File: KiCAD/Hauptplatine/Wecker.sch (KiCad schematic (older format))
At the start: 4 parts

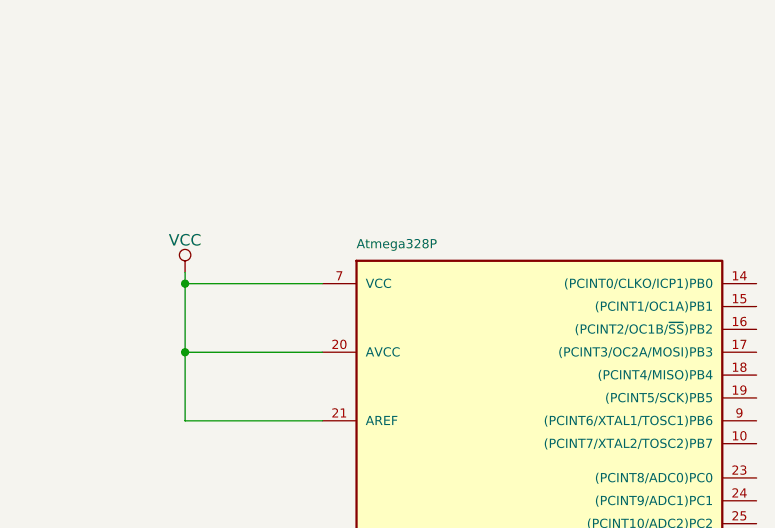
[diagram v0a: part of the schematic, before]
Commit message: Displayplatine Schematic erstellt
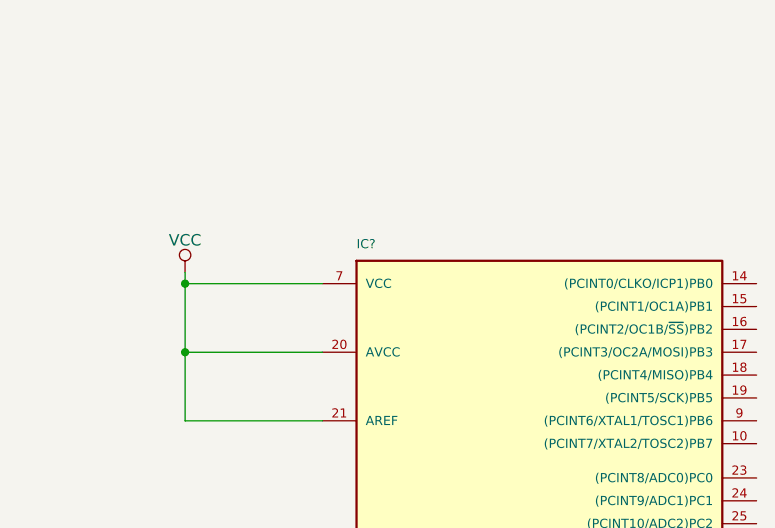
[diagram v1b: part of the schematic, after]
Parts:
- renumbered Atmega328P to IC?
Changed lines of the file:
@@
 $EndDescr
 $Comp
-L ATMEGA328P-P Atmega328P
+L ATMEGA328P-P IC?
 U 1 1 5627CFEE
 P 5750 3150
-F 0 "Atmega328P" H 5000 4400 40  0000 L BNN
+F 0 "IC?" H 5000 4400 40  0000 L BNN
 F 1 "ATMEGA328P-P" H 6150 1750 40  0000 L BNN
 F 2 "DIL28" H 5750 3150 30  0000 C CIN

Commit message: Hauptplatine inkl TDA7266
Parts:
- removed 33µ: C, symbol C
- added C? (x4): 100n, symbol C
- added C?: 33µ, symbol CP
- added P?: CONN_01X02, symbol CONN_01X02
- added P?: CONN_01X05, symbol CONN_01X05
- added P?: CONN_01X08, symbol CONN_01X08
- added R? (x4): R, symbol R
- added U?: TDA7266, TO220-15, symbol TDA7266
- C?: renamed from 47µ; value C -> 0,47µ
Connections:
- net GND: now also C?.1, C?.1, C?.1, C?.1, C?.2, R?.1, R?.1, R?.1, R?.1
- net VCC: now also C?.1, P?.2 (P2)
- net OSC2: now reaches IC?.10 ((PCINT7/XTAL2/TOSC2)PB7)
- net T1.1: now reaches IC?.15 ((PCINT1/OC1A)PB1)
- net T1.1: now also C?.2, P?.1 (P1), R?.2
- net DE-A: now reaches IC?.16 ((PCINT2/OC1B/~SS~)PB2)
- net DE-A: now also C?.2, P?.1 (P1), R?.2
- net DE-B: now reaches IC?.17 ((PCINT3/OC2A/MOSI)PB3)
- net DE-B: now also C?.2, P?.3 (P3), R?.2
- net DE-D: now reaches IC?.18 ((PCINT4/MISO)PB4)
- net DE-D: now also C?.2, P?.4 (P4), R?.2
- net DISP-A0: now reaches IC?.23 ((PCINT8/ADC0)PC0)
- net DISP-A0: now also IC?.26 ((PCINT11/ADC3)PC3), P?.3 (P3)
- net DISP-SCL: now reaches IC?.24 ((PCINT9/ADC1)PC1)
- net DISP-SCL: now also IC?.27 ((PCINT12/SDA/ADC4)PC4), P?.2 (P2)
- net DISP-SI: now reaches IC?.25 ((PCINT10/ADC2)PC2)
- net DISP-SI: now also IC?.28 ((PCINT13/SCL/ADC5)PC5), P?.1 (P1)
- net OSC1: now reaches IC?.9 ((PCINT6/XTAL1/TOSC1)PB6)
- new net DE-C: P?.2 (P2)
- new net DE-E: P?.5 (P5)
- new net DISP-CS1B: P?.5 (P5)
- new net DISP-GND: P?.7 (P7)
- new net DISP-LED: P?.6 (P6)
- new net DISP-RST: P?.4 (P4)
- new net DISP-VCC: P?.8 (P8)

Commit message: Layout Hauptplatine2 v1. Mp3Player-On falsch
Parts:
- removed C?: 100n, symbol C
- removed R?: R, symbol R
- added C10: 470uF, symbol CP
- added C11, C12: 0,22u, symbol C
- added C4: 100n, symbol C
- added C7, C8: 220nF, symbol CP
- added C9: 100nF, symbol C
- added P2: CONN_MP3Player, symbol CONN_01X08
- added P3: LED_Bilder, symbol CONN_01X02
- added P7, P8: CONN_01X02, symbol CONN_01X02
- added P9: CONN_OSC, symbol CONN_01X02
- added R3: R, symbol R
- added R5, R6, R7: 10k, symbol R
- added R8: 220, symbol R
- added U3: LM317T, symbol LM317T
- added U4: CBP, CBP:testneu, symbol CBP
- added U5: CBP, symbol CBP
- IC1: renamed from IC?; footprint DIL28 -> (none)
- P4: renamed from P?; value CONN_01X02 -> CONN_TASTER
- P5: renamed from P?; value CONN_01X05 -> CONN_DREHENCODER
- P6: renamed from P?; value CONN_01X08 -> CONN_DISPLAY
- U2: renamed from U?; footprint TO220-15 -> (none)
- gave numbers to parts that had none: 9
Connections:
- net labels added: Amp-Mute, Amp-Power, LED-Bilder, MP3-L, MP3-R, MP3-T1, MP3-T3, MP3-T4, MP3-T5, MP3_ON1, MP3_ON2, MP3_T1, MP3_T3, MP3_T4, MP3_T5, MP3_VCC, SPK-L+, SPK-L-, SPK-R+, SPK-R-, Transistor-Emitter, Transistorschaltung
- net labels removed: OSC1, OSC2
- wire segments 94 -> 174
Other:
- note added: "Audio-Verstärker"
- note added: "Connector Spannungsversorgung"
- note added: "Spannungsregler 1,5V"
- note added: "Spannungsregler 3,3V"
- moved on the sheet: C1, C2, C3, C5, C6, IC1, P4, P5, P6, R1, R2, R4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
